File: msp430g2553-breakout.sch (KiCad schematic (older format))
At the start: 25 parts, among them J1 Left, J2 Right, J3 SBW, Q1 BSS138, Q2 BSS138, SW1 Reset, U1 MSP430G2553IPW28, Y1 32.768kHz

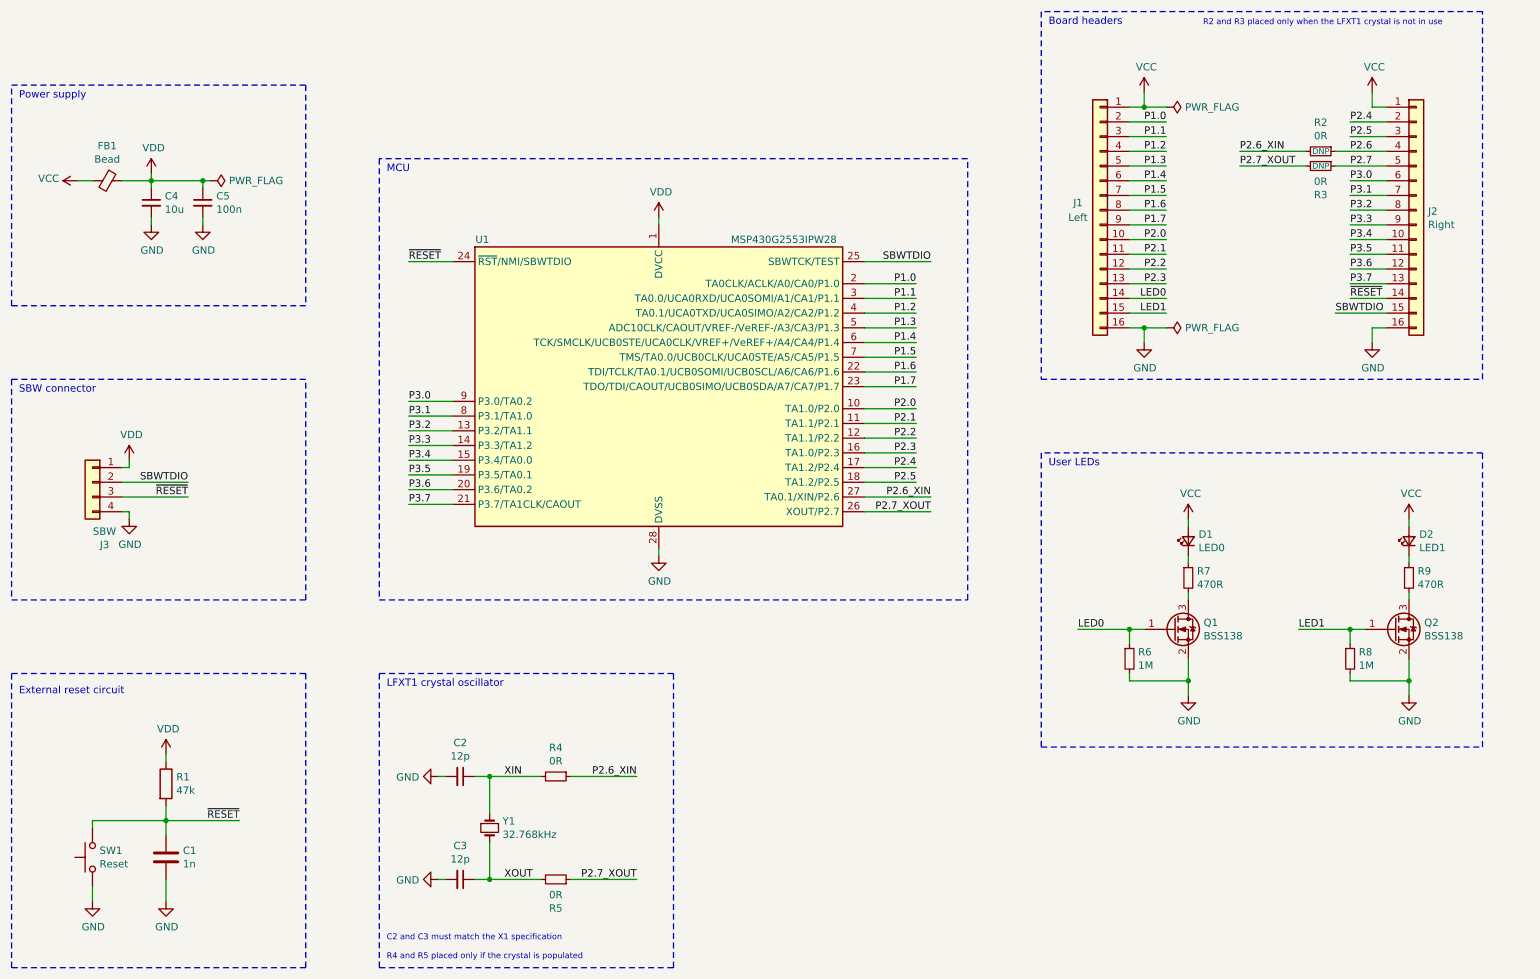
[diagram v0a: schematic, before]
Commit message: Fixed swapped SBWTDIO and SBWTCK pins, revision bump to A1
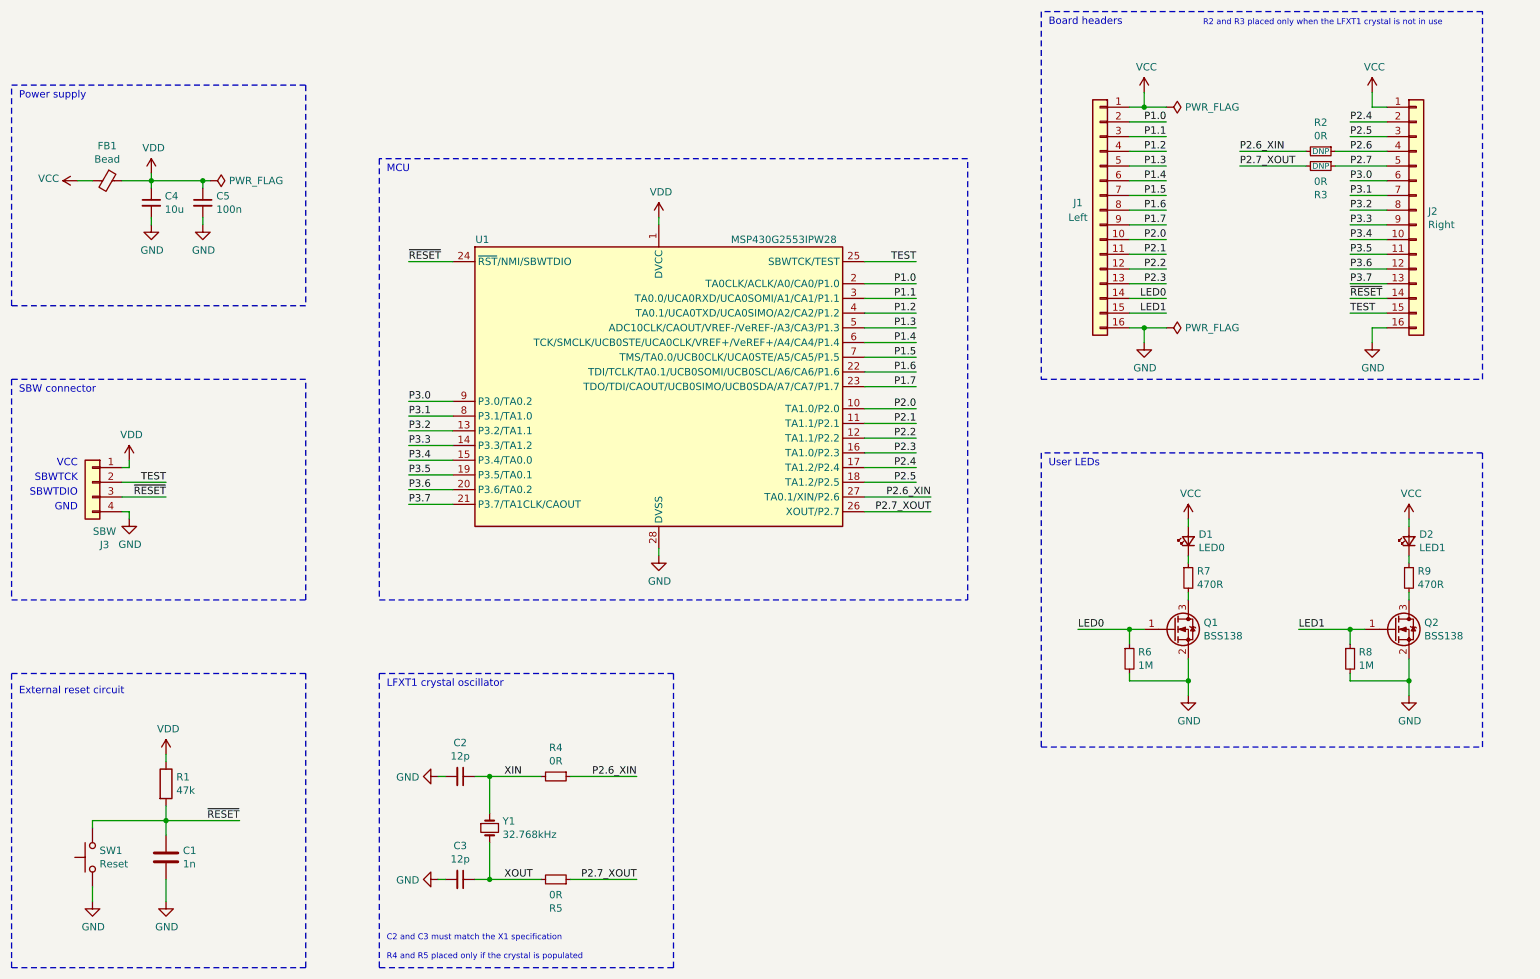
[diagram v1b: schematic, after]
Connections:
- net SBWTDIO renamed TEST
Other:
- note added: "GND"
- note added: "SBWTCK"
- note added: "SBWTDIO"
- note added: "VCC"
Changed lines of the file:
@@
 Sheet 1 1
 Title "MSP430G2553 Breakout Board"
-Date "2020-09-18"
-Rev "A"
+Date "2021-04-01"
+Rev "A1"
 Comp ""
 Comment1 "Mini breakout board for the MSP430G2553 microcontroller"
@@
 ~RESET
 Wire Wire Line
-	6800 2700 7250 2700
-Text Label 7250 2700 2    50   ~ 0
-SBWTDIO
+	6800 2700 7150 2700
+Text Label 7150 2700 2    50   ~ 0
+TEST
 Wire Wire Line
 	6800 2850 7150 2850
@@
 	10350 2950 10100 2950
 Wire Wire Line
-	10350 3050 10000 3050
+	10350 3050 10100 3050
 $Comp
 L power:GND #PWR09
@@
 Text Label 10100 2950 0    50   ~ 0
 ~RESET
-Text Label 10000 3050 0    50   ~ 0
-SBWTDIO
+Text Label 10100 3050 0    50   ~ 0
+TEST
 $Comp
 L Device:R_Small R2
@@
 Wire Wire Line
 	1750 4100 1800 4100
-Text Label 2200 4200 2    50   ~ 0
-SBWTDIO
-Text Label 2200 4300 2    50   ~ 0
+Text Label 2050 4200 2    50   ~ 0
+TEST
+Text Label 2050 4300 2    50   ~ 0
 ~RESET
 Wire Wire Line
-	1750 4200 2200 4200
-Wire Wire Line
-	1750 4300 2200 4300
+	1750 4200 2050 4200
+Wire Wire Line
+	1750 4300 2050 4300
 $Comp
 L power:PWR_FLAG #FLG0102
@@
 Text Notes 9100 1100 0    40   ~ 0
 R2 and R3 placed only when the LFXT1 crystal is not in use
+Text Notes 1450 4200 2    50   ~ 0
+SBWTCK
+Text Notes 1450 4300 2    50   ~ 0
+SBWTDIO
+Text Notes 1450 4100 2    50   ~ 0
+VCC
+Text Notes 1450 4400 2    50   ~ 0
+GND
 $EndSCHEMATC
